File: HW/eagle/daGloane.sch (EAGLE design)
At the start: 83 parts, among them IC1 MCP1252-33X50, U1 STM32F10XTXU6, X2 SPARKFUN-CONNECTORS_USB-MICROB

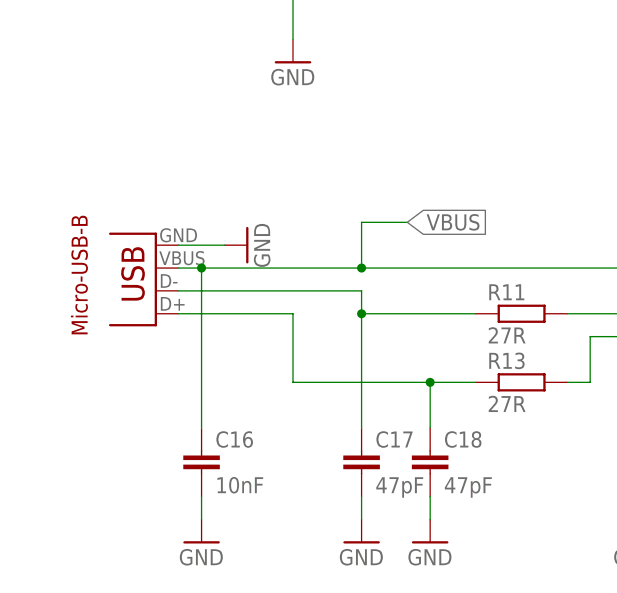
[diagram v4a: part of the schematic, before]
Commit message: - micro usb connector with electrical connection to mounting pad added - micro usb connector replaced with new part - micro usb connectors mounting pads' size increased with shape. This is to increase mechanical strength
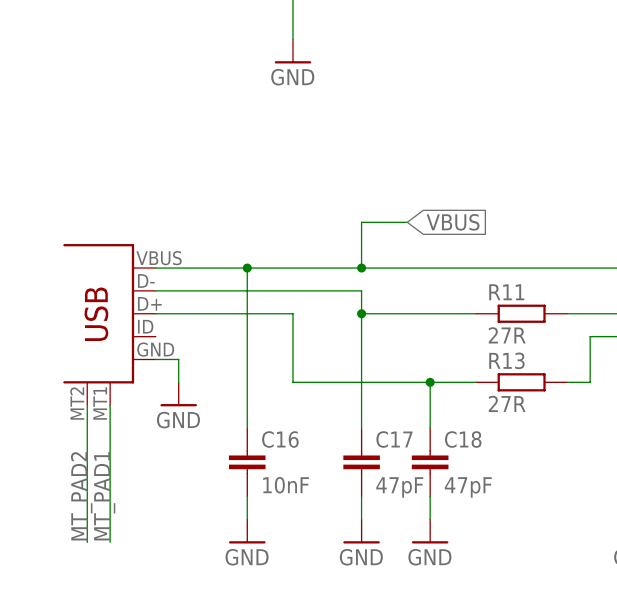
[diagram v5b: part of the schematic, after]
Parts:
- X2: value SPARKFUN-CONNECTORS_USB-MICROB -> USB_MICROB_PLUG_MT; device daGloane:SPARKFUN-CONNECTORS_USB-MICROB -> daGloane:USB_MICROB_PLUG_MT
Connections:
- new net MT_PAD1: X2.MTN1
- new net MT_PAD2: X2.MTN2
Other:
- note removed: "Micro-USB-B"
- moved on the sheet: C16
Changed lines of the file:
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@@
 <?xml version="1.0" encoding="utf-8"?>
 <!DOCTYPE eagle SYSTEM "eagle.dtd">
-<eagle version="6.2">
+<eagle version="6.1">
 <drawing>
 <settings>
@@
 <part name="GND1" library="supply1" deviceset="GND" device=""/>
 <part name="GND6" library="supply1" deviceset="GND" device=""/>
-<part name="X2" library="daGloane" deviceset="SPARKFUN-CONNECTORS_USB" device="-MICROB"/>
+<part name="X2" library="daGloane" deviceset="USB_MICROB_PLUG_MT" device=""/>
 <part name="C21" library="rcl" deviceset="C-EU" device="C0805" value="10µF/6.3V"/>
 <part name="3.3V1" library="supply1" deviceset="VCC" device="" value="3.3V"/>
@@
 <sheet>
 <plain>
-<text x="10.2" y="-350.48" size="1.778" layer="94" rot="R90">Micro-USB-B</text>
 <rectangle x1="295.45" y1="7.65" x2="335.75" y2="7.75" layer="201"/>
 <rectangle x1="295.45" y1="7.75" x2="335.75" y2="7.85" layer="201"/>
@@
 <instance part="GND12" gate="1" x="33.02" y="-320.04"/>
 <instance part="R17" gate="G$1" x="25.4" y="-294.64"/>
-<instance part="GND9" gate="1" x="27.94" y="-340.36" rot="R90"/>
+<instance part="GND9" gate="1" x="20.32" y="-358.14"/>
 <instance part="R12" gate="G$1" x="124.46" y="50.8" rot="MR90"/>
 <instance part="R21" gate="G$1" x="124.46" y="30.48" rot="MR90"/>
@@
 <instance part="GND5" gate="1" x="71.12" y="-373.38"/>
 <instance part="GND7" gate="1" x="83.82" y="-373.38"/>
-<instance part="C16" gate="G$1" x="22.86" y="-363.22"/>
-<instance part="GND8" gate="1" x="22.86" y="-373.38"/>
+<instance part="C16" gate="G$1" x="27.94" y="-363.22"/>
+<instance part="GND8" gate="1" x="27.94" y="-373.38"/>
 <instance part="C1" gate="G$1" x="320.04" y="218.44"/>
 <instance part="C15" gate="G$1" x="314.96" y="142.24" smashed="yes">
@@
 <instance part="GND1" gate="1" x="137.16" y="71.12" rot="MR0"/>
 <instance part="GND6" gate="1" x="116.84" y="17.78" rot="MR0"/>
-<instance part="X2" gate="G$1" x="17.78" y="-340.36" rot="R180"/>
+<instance part="X2" gate="G$1" x="10.16" y="-347.98" rot="MR0"/>
 <instance part="C21" gate="G$1" x="195.58" y="-292.1" rot="MR0"/>
 <instance part="3.3V1" gate="VCC" x="195.58" y="-281.94" rot="MR0"/>
@@
 </segment>
 <segment>
-<wire x1="20.32" y1="-340.36" x2="25.4" y2="-340.36" width="0.1524" layer="91"/>
+<wire x1="17.78" y1="-353.06" x2="20.32" y2="-353.06" width="0.1524" layer="91"/>
+<wire x1="20.32" y1="-353.06" x2="20.32" y2="-355.6" width="0.1524" layer="91"/>
 <pinref part="GND9" gate="1" pin="GND"/>
 <pinref part="X2" gate="G$1" pin="GND"/>
@@
 <pinref part="GND4" gate="1" pin="GND"/>
 <wire x1="40.64" y1="-370.84" x2="40.64" y2="-368.3" width="0.1524" layer="91"/>
-<wire x1="22.86" y1="-370.84" x2="22.86" y2="-368.3" width="0.1524" layer="91"/>
+<wire x1="27.94" y1="-370.84" x2="27.94" y2="-368.3" width="0.1524" layer="91"/>
 <pinref part="C16" gate="G$1" pin="2"/>
 <pinref part="GND8" gate="1" pin="GND"/>
@@
 <net name="D-" class="0">
 <segment>
-<wire x1="20.32" y1="-345.44" x2="40.64" y2="-345.44" width="0.1524" layer="91"/>
+<wire x1="17.78" y1="-345.44" x2="40.64" y2="-345.44" width="0.1524" layer="91"/>
 <wire x1="40.64" y1="-345.44" x2="40.64" y2="-347.98" width="0.1524" layer="91"/>
 <pinref part="R11" gate="G$1" pin="1"/>
@@
 <net name="D+" class="0">
 <segment>
-<wire x1="20.32" y1="-347.98" x2="33.02" y2="-347.98" width="0.1524" layer="91"/>
+<wire x1="17.78" y1="-347.98" x2="33.02" y2="-347.98" width="0.1524" layer="91"/>
 <wire x1="33.02" y1="-347.98" x2="33.02" y2="-355.6" width="0.1524" layer="91"/>
 <wire x1="33.02" y1="-355.6" x2="48.26" y2="-355.6" width="0.1524" layer="91"/>
@@
 <segment>
 <pinref part="U$4" gate="G$1" pin="VCC"/>
-<wire x1="20.32" y1="-342.9" x2="22.86" y2="-342.9" width="0.1524" layer="91"/>
+<wire x1="17.78" y1="-342.9" x2="27.94" y2="-342.9" width="0.1524" layer="91"/>
 <pinref part="C16" gate="G$1" pin="1"/>
-<wire x1="22.86" y1="-342.9" x2="40.64" y2="-342.9" width="0.1524" layer="91"/>
+<wire x1="27.94" y1="-342.9" x2="40.64" y2="-342.9" width="0.1524" layer="91"/>
 <wire x1="40.64" y1="-342.9" x2="86.36" y2="-342.9" width="0.1524" layer="91"/>
-<wire x1="22.86" y1="-360.68" x2="22.86" y2="-342.9" width="0.1524" layer="91"/>
-<junction x="22.86" y="-342.9"/>
+<wire x1="27.94" y1="-360.68" x2="27.94" y2="-342.9" width="0.1524" layer="91"/>
+<junction x="27.94" y="-342.9"/>
 <wire x1="40.64" y1="-342.9" x2="40.64" y2="-337.82" width="0.1524" layer="91"/>
 <wire x1="40.64" y1="-337.82" x2="45.72" y2="-337.82" width="0.1524" layer="91"/>
@@
 </segment>
 </net>
+<net name="MT_PAD2" class="0">
+<segment>
+<pinref part="X2" gate="G$1" pin="MTN2"/>
+<wire x1="10.16" y1="-358.14" x2="10.16" y2="-373.38" width="0.1524" layer="91"/>
+<label x="10.16" y="-373.38" size="1.778" layer="95" rot="R90"/>
+</segment>
+</net>
+<net name="MT_PAD1" class="0">
+<segment>
+<pinref part="X2" gate="G$1" pin="MTN1"/>
+<wire x1="12.7" y1="-358.14" x2="12.7" y2="-373.38" width="0.1524" layer="91"/>
+<label x="12.7" y="-373.38" size="1.778" layer="95" rot="R90"/>
+</segment>
+</net>

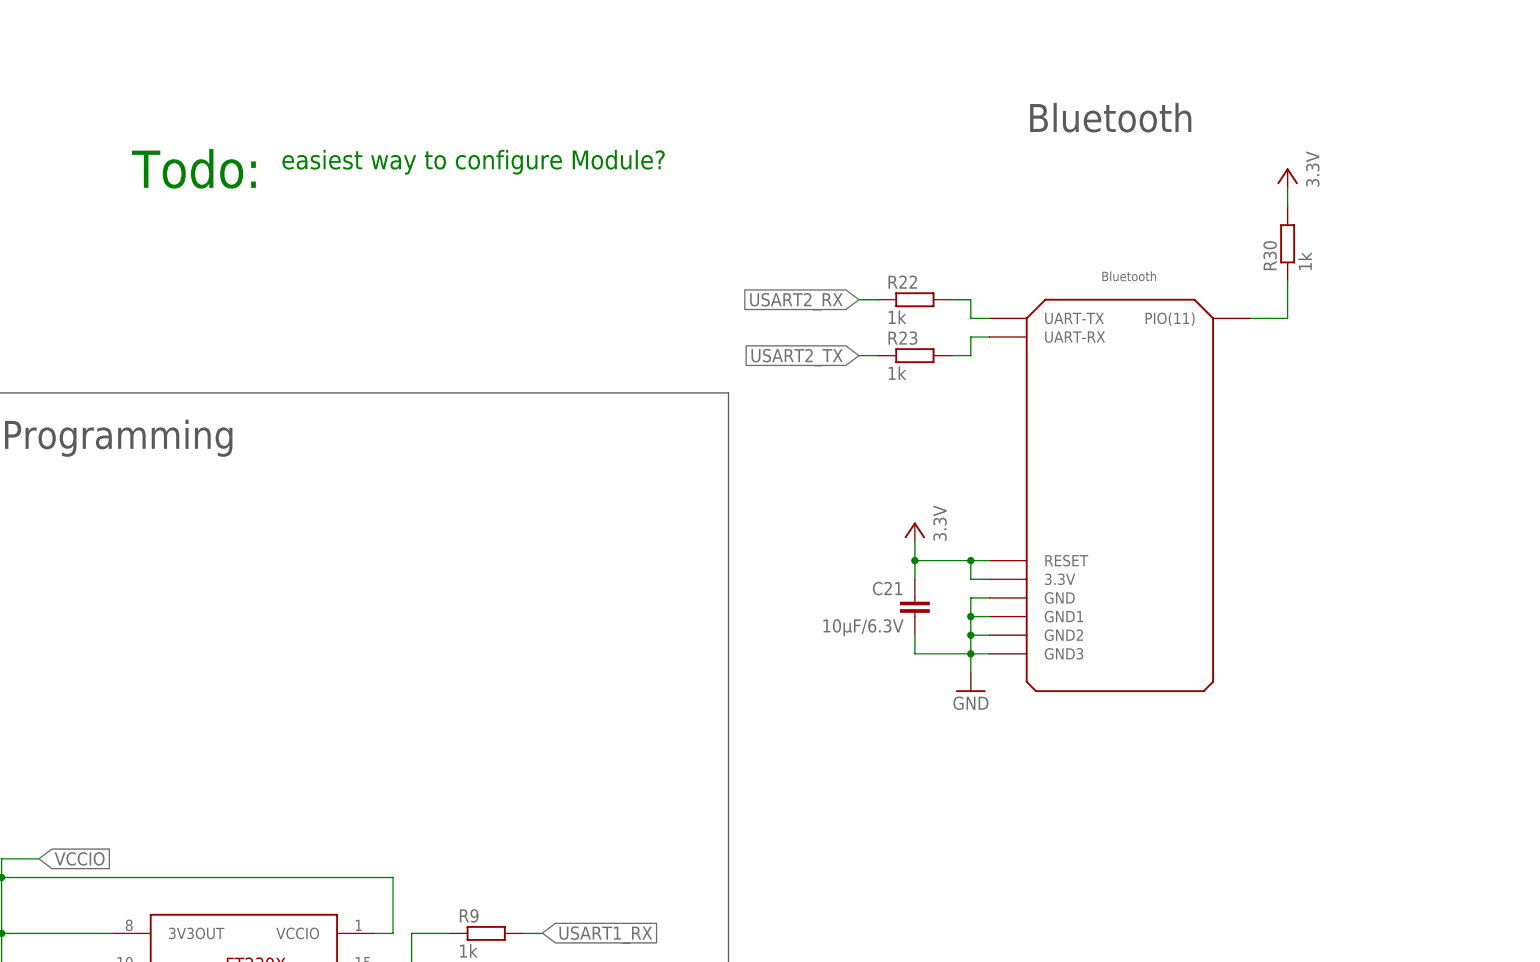
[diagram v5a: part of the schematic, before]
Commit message: changed connection of the bluetooth module's AT pin.
It is now connected to the pwr_on/off logic. This will set it into AT mode at startup so the µC can configure the module. Once the configuration is done the µC can set it into operating mode by simply sending a AT+RESET command.
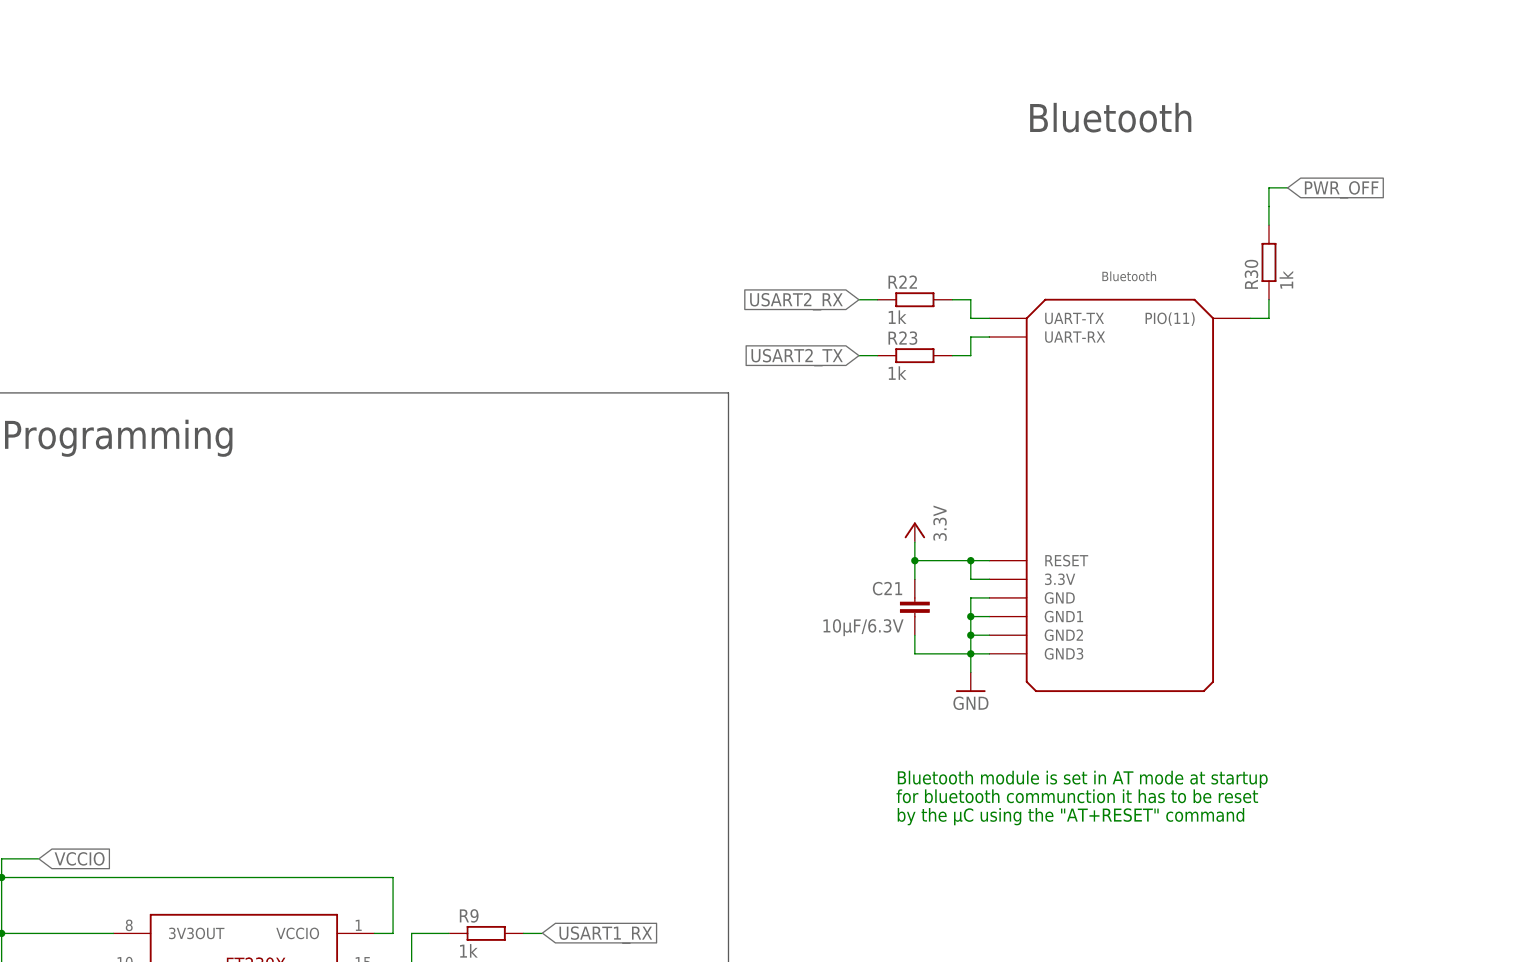
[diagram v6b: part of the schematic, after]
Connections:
- net PWR_OFF: now also R30.2
- net VCC: no longer R30.2
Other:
- note added: "Bluetooth module is set in AT mode at startup"
- note added: "by the µC using the "AT+RESET" command"
- note added: "for bluetooth communction it has to be reset"
- note removed: "Todo:"
- note removed: "easiest way to configure Module?"
- moved on the sheet: R30
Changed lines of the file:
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@@
 <part name="U$9" library="daGloane" deviceset="3A_BLDC_CONTROLLER" device=""/>
 <part name="R28" library="rcl" deviceset="R-EU_" device="R0603" value="10k"/>
-<part name="3.3V7" library="supply1" deviceset="VCC" device="" value="3.3V"/>
 <part name="U$5" library="daGloane" deviceset="BLUETOOTH_REDUCED" device=""/>
 <part name="R30" library="rcl" deviceset="R-EU_" device="R0603" value="1k"/>
@@
 <wire x1="215.9" y1="243.84" x2="215.9" y2="111.76" width="0.1524" layer="97"/>
 <wire x1="215.9" y1="111.76" x2="342.9" y2="111.76" width="0.1524" layer="97"/>
-<text x="88.9" y="-236.22" size="5.08" layer="91">Todo:</text>
-<text x="109.22" y="-233.68" size="2.54" layer="91">easiest way to configure Module?</text>
 <text x="444.5" y="-175.26" size="5.08" layer="94">BLDC Controllers</text>
+<text x="193.04" y="-317.5" size="1.778" layer="91">Bluetooth module is set in AT mode at startup</text>
+<text x="193.04" y="-320.04" size="1.778" layer="91">for bluetooth communction it has to be reset </text>
+<text x="193.04" y="-322.58" size="1.778" layer="91">by the µC using the "AT+RESET" command</text>
 </plain>
 <instances>
@@
 <instance part="U$9" gate="G$1" x="497.84" y="-121.92"/>
 <instance part="R28" gate="G$1" x="137.16" y="81.28" rot="R90"/>
-<instance part="3.3V7" gate="VCC" x="246.38" y="-233.68" rot="MR0"/>
 <instance part="U$5" gate="G$1" x="223.52" y="-276.86"/>
-<instance part="R30" gate="G$1" x="246.38" y="-243.84" rot="R90"/>
+<instance part="R30" gate="G$1" x="243.84" y="-246.38" rot="R90"/>
 </instances>
 <busses>
@@
 <pinref part="3.3V5" gate="VCC" pin="VCC"/>
 </segment>
-<segment>
-<pinref part="3.3V7" gate="VCC" pin="VCC"/>
-<wire x1="246.38" y1="-236.22" x2="246.38" y2="-238.76" width="0.1524" layer="91"/>
-<pinref part="R30" gate="G$1" pin="2"/>
-</segment>
 </net>
 <net name="USART_RX1" class="0">
@@
 <label x="119.38" y="165.1" size="1.778" layer="95" xref="yes"/>
 </segment>
+<segment>
+<wire x1="246.38" y1="-236.22" x2="243.84" y2="-236.22" width="0.1524" layer="91"/>
+<wire x1="243.84" y1="-236.22" x2="243.84" y2="-238.76" width="0.1524" layer="91"/>
+<wire x1="243.84" y1="-238.76" x2="243.84" y2="-241.3" width="0.1524" layer="91"/>
+<pinref part="R30" gate="G$1" pin="2"/>
+<label x="246.38" y="-236.22" size="1.778" layer="95" xref="yes"/>
+</segment>
 </net>
 <net name="N$23" class="0">
@@
 <net name="N$26" class="0">
 <segment>
-<wire x1="246.38" y1="-248.92" x2="246.38" y2="-254" width="0.1524" layer="91"/>
-<wire x1="246.38" y1="-254" x2="241.3" y2="-254" width="0.1524" layer="91"/>
+<wire x1="243.84" y1="-251.46" x2="243.84" y2="-254" width="0.1524" layer="91"/>
+<wire x1="243.84" y1="-254" x2="241.3" y2="-254" width="0.1524" layer="91"/>
 <pinref part="U$5" gate="G$1" pin="PIO(11)"/>
 <pinref part="R30" gate="G$1" pin="1"/>

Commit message: stm32 vqfpn36 package cream layer divided in 4 segments
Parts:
- C4: value 1µF -> 4.7
- C6: value 1µF -> 4.7µF
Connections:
- net LIPO: now also IC1.SELECT
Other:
- moved on the sheet: GND, SWCLK, SWDIO
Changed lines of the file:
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@@
 <part name="LED2" library="led" deviceset="LED" device="CHIPLED_0603"/>
 <part name="U$2" library="daGloane" deviceset="SPARKFUN_MCP73831" device=""/>
-<part name="C6" library="rcl" deviceset="C-EU" device="C0603" value="1µF"/>
+<part name="C6" library="rcl" deviceset="C-EU" device="C0603" value="4.7µF"/>
 <part name="GND28" library="supply1" deviceset="GND" device=""/>
 <part name="GND29" library="supply1" deviceset="GND" device=""/>
-<part name="C4" library="rcl" deviceset="C-EU" device="C0603" value="1µF"/>
+<part name="C4" library="rcl" deviceset="C-EU" device="C0603" value="4.7"/>
 <part name="GND30" library="supply1" deviceset="GND" device=""/>
 <part name="LIPO+" library="testpad" deviceset="TPS" device="PAD1-13"/>
@@
 <instance part="FRAME2" gate="G$1" x="0" y="0"/>
 <instance part="3.3V" gate="VCC" x="33.02" y="-274.32"/>
-<instance part="SWDIO" gate="G$1" x="20.32" y="30.48" smashed="yes" rot="R90">
-<attribute name="NAME" x="11.176" y="30.988" size="1.778" layer="95"/>
+<instance part="SWDIO" gate="G$1" x="106.68" y="-292.1" smashed="yes" rot="R90">
+<attribute name="NAME" x="97.536" y="-291.592" size="1.778" layer="95"/>
 </instance>
-<instance part="SWCLK" gate="G$1" x="20.32" y="25.4" smashed="yes" rot="R90">
-<attribute name="NAME" x="11.176" y="25.908" size="1.778" layer="95"/>
+<instance part="SWCLK" gate="G$1" x="106.68" y="-297.18" smashed="yes" rot="R90">
+<attribute name="NAME" x="97.536" y="-296.672" size="1.778" layer="95"/>
 </instance>
-<instance part="GND" gate="G$1" x="20.32" y="20.32" smashed="yes" rot="R90">
-<attribute name="NAME" x="11.176" y="20.828" size="1.778" layer="95"/>
+<instance part="GND" gate="G$1" x="106.68" y="-302.26" smashed="yes" rot="R90">
+<attribute name="NAME" x="97.536" y="-301.752" size="1.778" layer="95"/>
 </instance>
-<instance part="GND2" gate="1" x="27.94" y="15.24"/>
+<instance part="GND2" gate="1" x="114.3" y="-307.34"/>
 <instance part="U$3" gate="G$1" x="307.34" y="177.8"/>
 <instance part="U$4" gate="G$1" x="104.14" y="-350.52"/>
@@
 <segment>
 <pinref part="GND" gate="G$1" pin="TP"/>
-<wire x1="22.86" y1="20.32" x2="27.94" y2="20.32" width="0.1524" layer="91"/>
-<wire x1="27.94" y1="20.32" x2="27.94" y2="17.78" width="0.1524" layer="91"/>
+<wire x1="109.22" y1="-302.26" x2="114.3" y2="-302.26" width="0.1524" layer="91"/>
+<wire x1="114.3" y1="-302.26" x2="114.3" y2="-304.8" width="0.1524" layer="91"/>
 <pinref part="GND2" gate="1" pin="GND"/>
 </segment>
@@
 <pinref part="U$9" gate="G$1" pin="ACCU+"/>
 </segment>
+<segment>
+<pinref part="IC1" gate="G$1" pin="SELECT"/>
+<wire x1="210.82" y1="-81.28" x2="213.36" y2="-81.28" width="0.1524" layer="91"/>
+<wire x1="213.36" y1="-81.28" x2="213.36" y2="-68.58" width="0.1524" layer="91"/>
+<label x="213.36" y="-68.58" size="1.778" layer="95" rot="R90" xref="yes"/>
+</segment>
 </net>
 <net name="VOLTAGE" class="0">
@@
 <segment>
 <pinref part="SWDIO" gate="G$1" pin="TP"/>
-<wire x1="22.86" y1="30.48" x2="27.94" y2="30.48" width="0.1524" layer="91"/>
-<label x="27.94" y="30.48" size="1.778" layer="95" xref="yes"/>
+<wire x1="109.22" y1="-292.1" x2="114.3" y2="-292.1" width="0.1524" layer="91"/>
+<label x="114.3" y="-292.1" size="1.778" layer="95" xref="yes"/>
 </segment>
 <segment>
@@
 <segment>
 <pinref part="SWCLK" gate="G$1" pin="TP"/>
-<wire x1="22.86" y1="25.4" x2="27.94" y2="25.4" width="0.1524" layer="91"/>
-<label x="27.94" y="25.4" size="1.778" layer="95" xref="yes"/>
-</segment>
-<segment>
+<wire x1="109.22" y1="-297.18" x2="114.3" y2="-297.18" width="0.1524" layer="91"/>
+<label x="114.3" y="-297.18" size="1.778" layer="95" xref="yes"/>
+</segment>
+<segment>
